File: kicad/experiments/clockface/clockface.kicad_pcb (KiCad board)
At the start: 2 copper layers, 50 x 50 mm, 11 parts, among them P1 CONN_01X05, U1 TOUCH_PAD_13, U2 MTCH6102_SSOP

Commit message: gerbers
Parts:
- moved R5 0.40 mm to (147.6, 102.8)
- moved R2 0.28 mm to (147.6, 100.5)
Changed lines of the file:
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@@
     (links 40)
     (no_connects 0)
-    (area 122.741999 68.527999 172.892001 118.678001)
+    (area 122.741999 67.691 172.892001 120.021)
     (thickness 1.6)
     (drawings 25)
@@
   )
   (module Resistors_SMD:R_0805_HandSoldering (layer B.Cu)
-    (at 147.74164 100.78974 180)
+    (at 147.61464 100.53574 180)
     (descr "Resistor SMD 0805, hand soldering")
     (tags "resistor 0805")
@@
   )
   (module Resistors_SMD:R_0805_HandSoldering (layer B.Cu)
-    (at 147.74164 103.20274 180)
+    (at 147.61464 102.82174 180)
     (descr "Resistor SMD 0805, hand soldering")
     (tags "resistor 0805")
@@
   (segment (start 153.166 96.778) (end 153.416 97.028) (width 0.305) (layer B.Cu) (net 10))
   (segment (start 153.416 97.028) (end 153.416 103.124) (width 0.305) (layer B.Cu) (net 10))
-  (segment (start 153.416 103.124) (end 151.384 105.156) (width 0.305) (layer B.Cu) (net 10))
-  (segment (start 151.384 105.156) (end 139.053401 105.156) (width 0.305) (layer B.Cu) (net 10))
-  (segment (start 139.053401 105.156) (end 135.016601 101.1192) (width 0.305) (layer B.Cu) (net 10))
+  (segment (start 153.416 103.124) (end 150.876 105.664) (width 0.305) (layer B.Cu) (net 10))
+  (segment (start 150.876 105.664) (end 139.561401 105.664) (width 0.305) (layer B.Cu) (net 10))
+  (segment (start 139.561401 105.664) (end 135.016601 101.1192) (width 0.305) (layer B.Cu) (net 10))
   (segment (start 151.301 96.778) (end 153.166 96.778) (width 0.305) (layer B.Cu) (net 10))
   (segment (start 135.016601 101.1192) (end 132.204801 103.931) (width 0.305) (layer F.Cu) (net 10))
@@
   (segment (start 147.869001 73.931) (end 147.869001 79.135861) (width 0.305) (layer F.Cu) (net 19))
   (segment (start 147.869001 79.135861) (end 147.93214 79.199) (width 0.305) (layer F.Cu) (net 19))
-  (segment (start 151.301 90.278) (end 152.8 90.278) (width 0.305) (layer B.Cu) (net 19) (status 400000))
+  (segment (start 151.301 90.278) (end 152.8 90.278) (width 0.305) (layer B.Cu) (net 19))
   (segment (start 150.827 79.199) (end 147.93214 79.199) (width 0.305) (layer B.Cu) (net 19))
   (segment (start 147.93214 79.199) (end 147.869001 79.199) (width 0.305) (layer B.Cu) (net 19))

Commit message: Soldermask on the ic footprint
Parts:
- P1: footprint SMD_Header_Straight_1x05 -> clockface:SMD_Header_Straight_1x05
- U1: footprint CPA_12 -> clockface:CPA_12
- U2: footprint Housings_SSOP:SSOP-28_5.3x10.2mm_Pitch0.65mm -> clockface:SSOP-28_5.3x10.2mm_Pitch0.65mm_masked

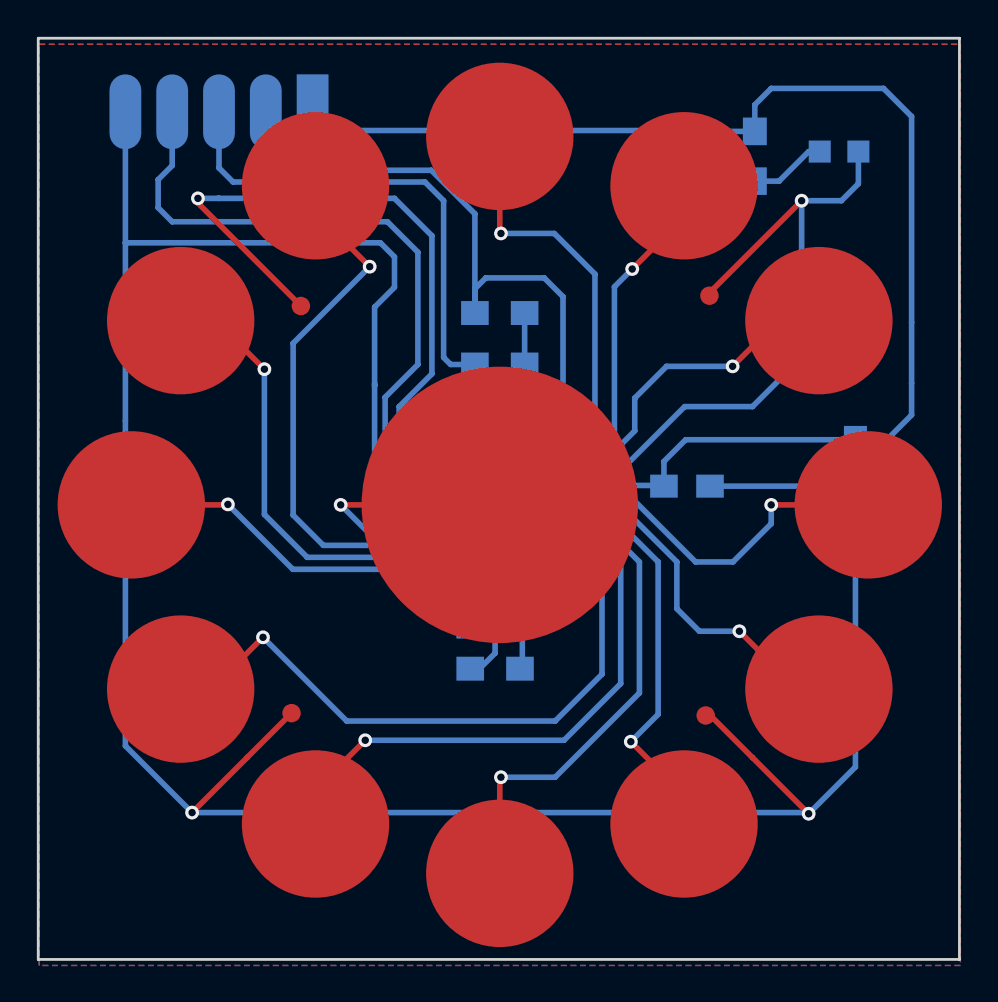
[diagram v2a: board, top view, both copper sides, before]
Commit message: Moved ground vias
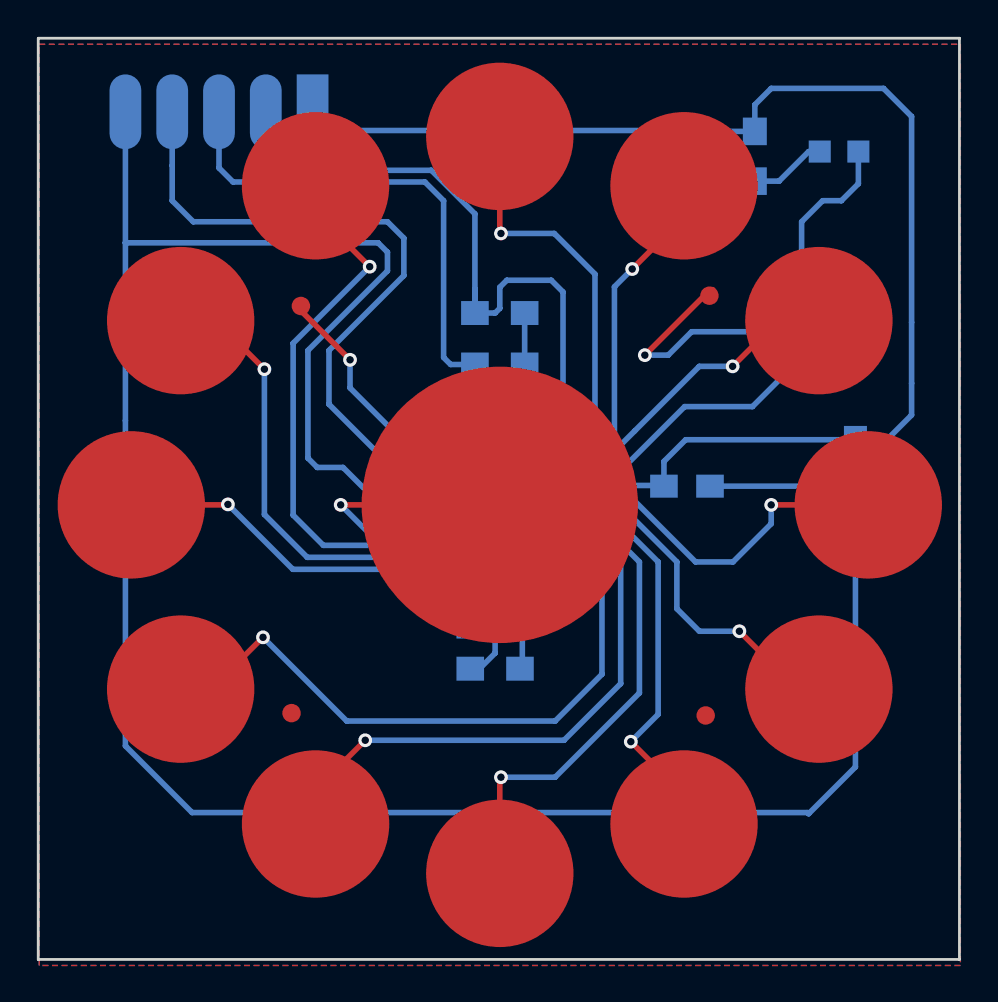
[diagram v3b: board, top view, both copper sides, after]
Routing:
- net GND: track 219.7 -> 190.4 mm, vias 4 -> 2
- net /SCL: track 33.3 -> 34.5 mm
- net /RX2: track 18.1 -> 17.1 mm
- net /INT: track 48.7 -> 49.7 mm

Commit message: Wider VCC track
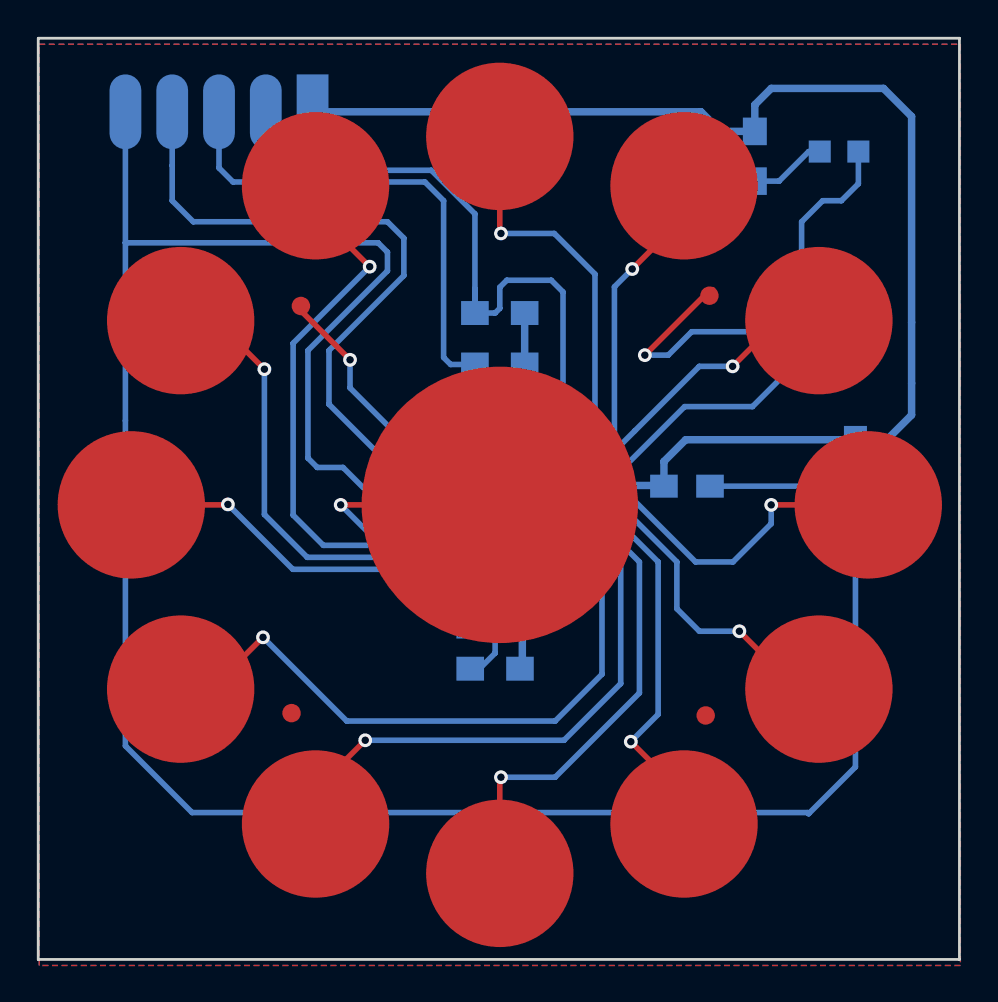
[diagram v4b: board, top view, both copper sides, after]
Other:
- net class VCC added: clearance 0.2, trace_width 0.406, via_dia 0.75, via_drill 0.4
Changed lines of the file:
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@@
     (links 40)
     (no_connects 1)
-    (area 122.741999 68.527999 172.892001 118.678001)
+    (area 122.741999 67.691 172.892001 120.021)
     (thickness 1.6)
     (drawings 26)
@@
     (uvia_dia 0.3)
     (uvia_drill 0.1)
-    (add_net /3V3)
     (add_net /INT)
     (add_net /RX0)
@@
     (add_net "Net-(U2-Pad6)")
     (add_net "Net-(U2-Pad9)")
+  )
+  (net_class VCC ""
+    (clearance 0.2)
+    (trace_width 0.406)
+    (via_dia 0.75)
+    (via_drill 0.4)
+    (uvia_dia 0.3)
+    (uvia_drill 0.1)
+    (add_net /3V3)
   )
   (module Capacitors_SMD:C_0805_HandSoldering (layer B.Cu)
@@
   (segment (start 142.3999 94.178) (end 144.101 94.178) (width 0.305) (layer B.Cu) (net 1))
   (segment (start 142.28064 94.05874) (end 142.3999 94.178) (width 0.305) (layer B.Cu) (net 1))
-  (segment (start 142.28064 93.86824) (end 142.28064 94.05874) (width 0.305) (layer B.Cu) (net 1) (status 2))
+  (segment (start 142.28064 93.86824) (end 142.28064 94.05874) (width 0.305) (layer B.Cu) (net 1))
   (segment (start 161.71164 76.35874) (end 163.02864 76.35874) (width 0.305) (layer B.Cu) (net 2))
   (segment (start 164.63264 74.75474) (end 165.23462 74.75474) (width 0.305) (layer B.Cu) (net 2))
@@
   (segment (start 146.51864 82.20074) (end 146.51864 83.51774) (width 0.305) (layer B.Cu) (net 5))
   (segment (start 130.08864 73.61174) (end 130.08864 75.51674) (width 0.305) (layer B.Cu) (net 6))
-  (segment (start 141.7049 91.578) (end 144.101 91.578) (width 0.305) (layer B.Cu) (net 6) (status 800000))
+  (segment (start 141.7049 91.578) (end 144.101 91.578) (width 0.305) (layer B.Cu) (net 6))
   (segment (start 138.59764 88.47074) (end 141.7049 91.578) (width 0.305) (layer B.Cu) (net 6))
   (segment (start 138.59764 85.54974) (end 138.59764 88.47074) (width 0.305) (layer B.Cu) (net 6))
@@
   (segment (start 153.035 90.043) (end 153.035 81.407) (width 0.305) (layer B.Cu) (net 19))
   (segment (start 152.8 90.278) (end 153.035 90.043) (width 0.305) (layer B.Cu) (net 19))
-  (segment (start 167.17264 90.39574) (end 168.87984 90.39574) (width 0.305) (layer B.Cu) (net 26))
-  (segment (start 170.22064 87.32774) (end 170.22064 84.02574) (width 0.305) (layer B.Cu) (net 26))
-  (segment (start 161.71164 72.21474) (end 161.71164 73.65874) (width 0.305) (layer B.Cu) (net 26))
-  (segment (start 162.60064 71.32574) (end 161.71164 72.21474) (width 0.305) (layer B.Cu) (net 26))
-  (segment (start 168.69664 71.32574) (end 162.60064 71.32574) (width 0.305) (layer B.Cu) (net 26))
-  (segment (start 170.22064 72.84974) (end 168.69664 71.32574) (width 0.305) (layer B.Cu) (net 26))
-  (segment (start 170.22064 84.02574) (end 170.22064 72.84974) (width 0.305) (layer B.Cu) (net 26))
-  (segment (start 170.22064 89.05494) (end 170.22064 87.32774) (width 0.305) (layer B.Cu) (net 26))
-  (segment (start 168.87984 90.39574) (end 170.22064 89.05494) (width 0.305) (layer B.Cu) (net 26))
-  (segment (start 156.77864 92.91574) (end 156.77864 91.57494) (width 0.305) (layer B.Cu) (net 26))
-  (segment (start 157.95784 90.39574) (end 167.17264 90.39574) (width 0.305) (layer B.Cu) (net 26))
-  (segment (start 156.77864 91.57494) (end 157.95784 90.39574) (width 0.305) (layer B.Cu) (net 26))
-  (segment (start 137.70864 73.61174) (end 158.51664 73.61174) (width 0.305) (layer B.Cu) (net 26))
-  (segment (start 158.51664 73.61174) (end 158.56364 73.65874) (width 0.305) (layer B.Cu) (net 26))
-  (segment (start 158.56364 73.65874) (end 161.71164 73.65874) (width 0.305) (layer B.Cu) (net 26))
-  (segment (start 158.51664 73.61174) (end 158.53664 73.63174) (width 0.305) (layer B.Cu) (net 26))
+  (segment (start 137.70864 72.59574) (end 158.79064 72.59574) (width 0.406) (layer B.Cu) (net 26) (status 400000))
+  (segment (start 159.85364 73.65874) (end 161.71164 73.65874) (width 0.406) (layer B.Cu) (net 26) (status 800000))
+  (segment (start 158.79064 72.59574) (end 159.85364 73.65874) (width 0.406) (layer B.Cu) (net 26))
+  (segment (start 151.301 92.878) (end 149.12938 92.878) (width 0.406) (layer B.Cu) (net 26) (status 400000))
+  (segment (start 149.12938 92.878) (end 149.09164 92.91574) (width 0.406) (layer B.Cu) (net 26))
+  (segment (start 167.17264 90.39574) (end 168.87984 90.39574) (width 0.406) (layer B.Cu) (net 26))
+  (segment (start 168.87984 90.39574) (end 170.22064 89.05494) (width 0.406) (layer B.Cu) (net 26))
+  (segment (start 170.22064 89.05494) (end 170.22064 87.32774) (width 0.406) (layer B.Cu) (net 26))
+  (segment (start 170.22064 84.02574) (end 170.22064 72.84974) (width 0.406) (layer B.Cu) (net 26))
+  (segment (start 170.22064 72.84974) (end 168.69664 71.32574) (width 0.406) (layer B.Cu) (net 26))
+  (segment (start 168.69664 71.32574) (end 162.60064 71.32574) (width 0.406) (layer B.Cu) (net 26))
+  (segment (start 162.60064 71.32574) (end 161.71164 72.21474) (width 0.406) (layer B.Cu) (net 26))
+  (segment (start 161.71164 72.21474) (end 161.71164 73.65874) (width 0.406) (layer B.Cu) (net 26))
+  (segment (start 170.22064 87.32774) (end 170.22064 84.02574) (width 0.406) (layer B.Cu) (net 26))
+  (segment (start 156.77864 92.91574) (end 156.77864 91.57494) (width 0.406) (layer B.Cu) (net 26))
+  (segment (start 156.77864 91.57494) (end 157.95784 90.39574) (width 0.406) (layer B.Cu) (net 26))
+  (segment (start 157.95784 90.39574) (end 167.17264 90.39574) (width 0.406) (layer B.Cu) (net 26))
   (segment (start 161.48464 73.88574) (end 161.71164 73.65874) (width 0.305) (layer B.Cu) (net 26))
-  (segment (start 149.09164 100.78974) (end 149.09164 103.20274) (width 0.305) (layer B.Cu) (net 26))
-  (segment (start 149.21864 86.31174) (end 149.21864 83.51774) (width 0.305) (layer B.Cu) (net 26))
-  (segment (start 149.09164 92.91574) (end 151.26326 92.91574) (width 0.305) (layer B.Cu) (net 26))
+  (segment (start 149.09164 100.78974) (end 149.09164 103.20274) (width 0.406) (layer B.Cu) (net 26))
+  (segment (start 149.21864 86.31174) (end 149.21864 83.51774) (width 0.406) (layer B.Cu) (net 26))
   (segment (start 151.26326 92.91574) (end 151.301 92.878) (width 0.305) (layer B.Cu) (net 26))
-  (segment (start 149.09164 100.78974) (end 149.09164 92.91574) (width 0.305) (layer B.Cu) (net 26))
-  (segment (start 149.09164 92.91574) (end 149.09164 86.43874) (width 0.305) (layer B.Cu) (net 26))
+  (segment (start 149.09164 100.78974) (end 149.09164 92.91574) (width 0.406) (layer B.Cu) (net 26))
+  (segment (start 149.09164 92.91574) (end 149.09164 86.43874) (width 0.406) (layer B.Cu) (net 26))
   (segment (start 149.09164 86.43874) (end 149.21864 86.31174) (width 0.305) (layer B.Cu) (net 26))
-  (segment (start 151.301 92.878) (end 156.7409 92.878) (width 0.305) (layer B.Cu) (net 26))
+  (segment (start 151.301 92.878) (end 156.7409 92.878) (width 0.406) (layer B.Cu) (net 26))
   (segment (start 156.7409 92.878) (end 156.77864 92.91574) (width 0.305) (layer B.Cu) (net 26))
   (zone (net 1) (net_name GND) (layer B.Cu) (hatch edge 0.508)

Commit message: Moved ground vias
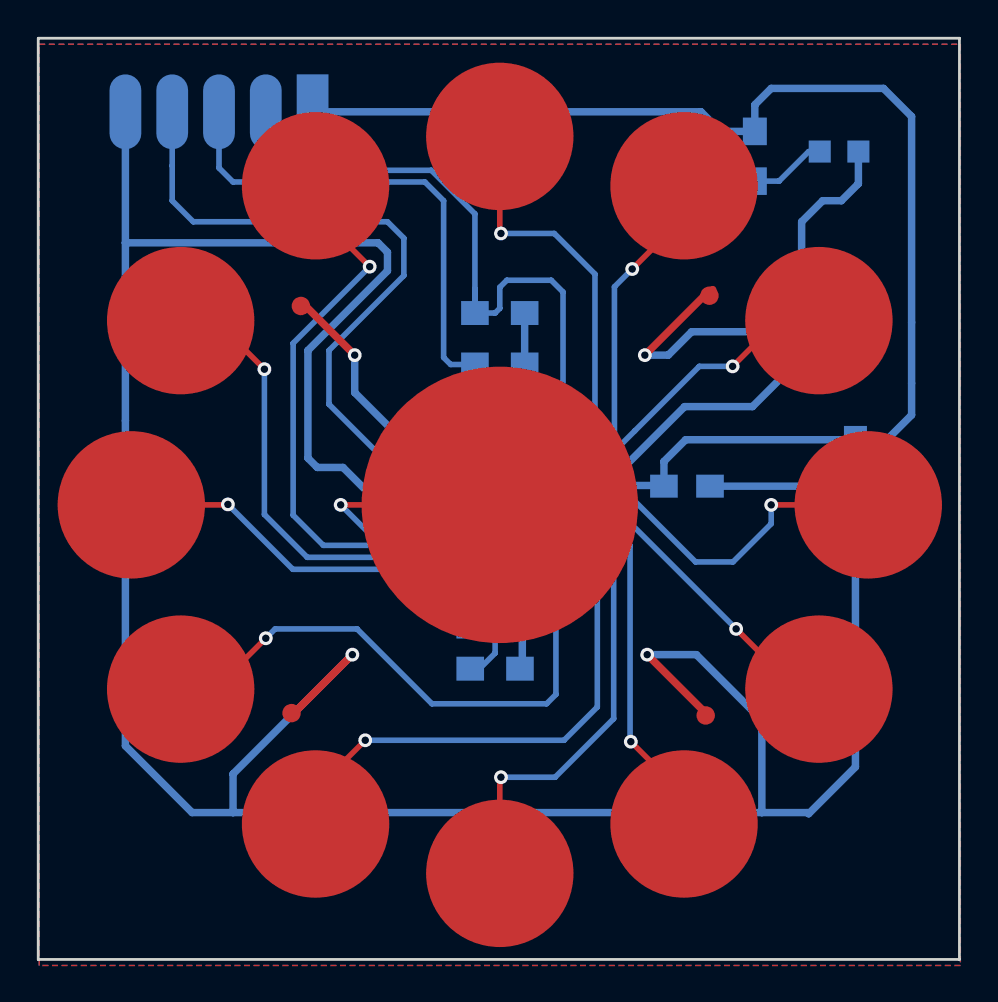
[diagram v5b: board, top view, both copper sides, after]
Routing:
- net GND: track 190.4 -> 224.0 mm, vias 2 -> 4
- net /RX6: track 26.6 -> 25.1 mm
- net /RX5: track 22.1 -> 20.6 mm
- net /RX7: track 30.9 -> 29.5 mm
- net /RX8: track 35.3 -> 34.6 mm
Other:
- net class GND added: clearance 0.2, trace_width 0.406, via_dia 0.75, via_drill 0.4
